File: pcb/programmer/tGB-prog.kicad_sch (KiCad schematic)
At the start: 34 parts, among them J1 ZX62R-B-5P, J2 PROG_PORT, U1 FT2232D, U2 93LC56BT-I/OT, U3 TPS79901DDCR, Y1 NX8045GB-6MHZ-STD-CSF-3

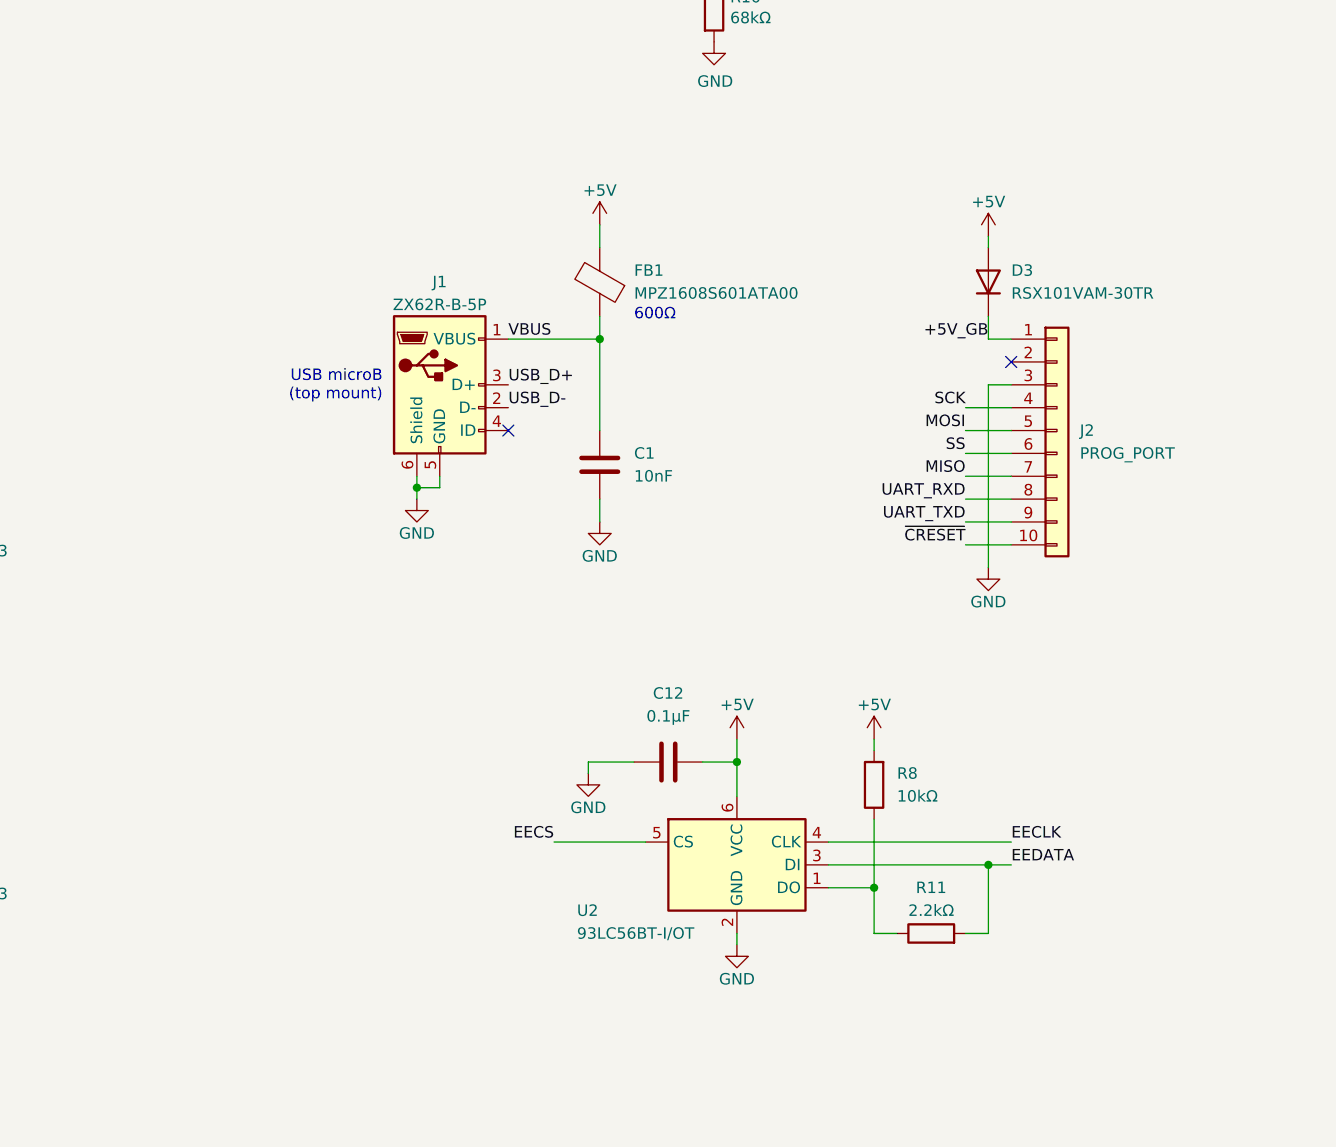
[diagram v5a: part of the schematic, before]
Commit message: add junpers for VDDIO supply from main board, add power LED
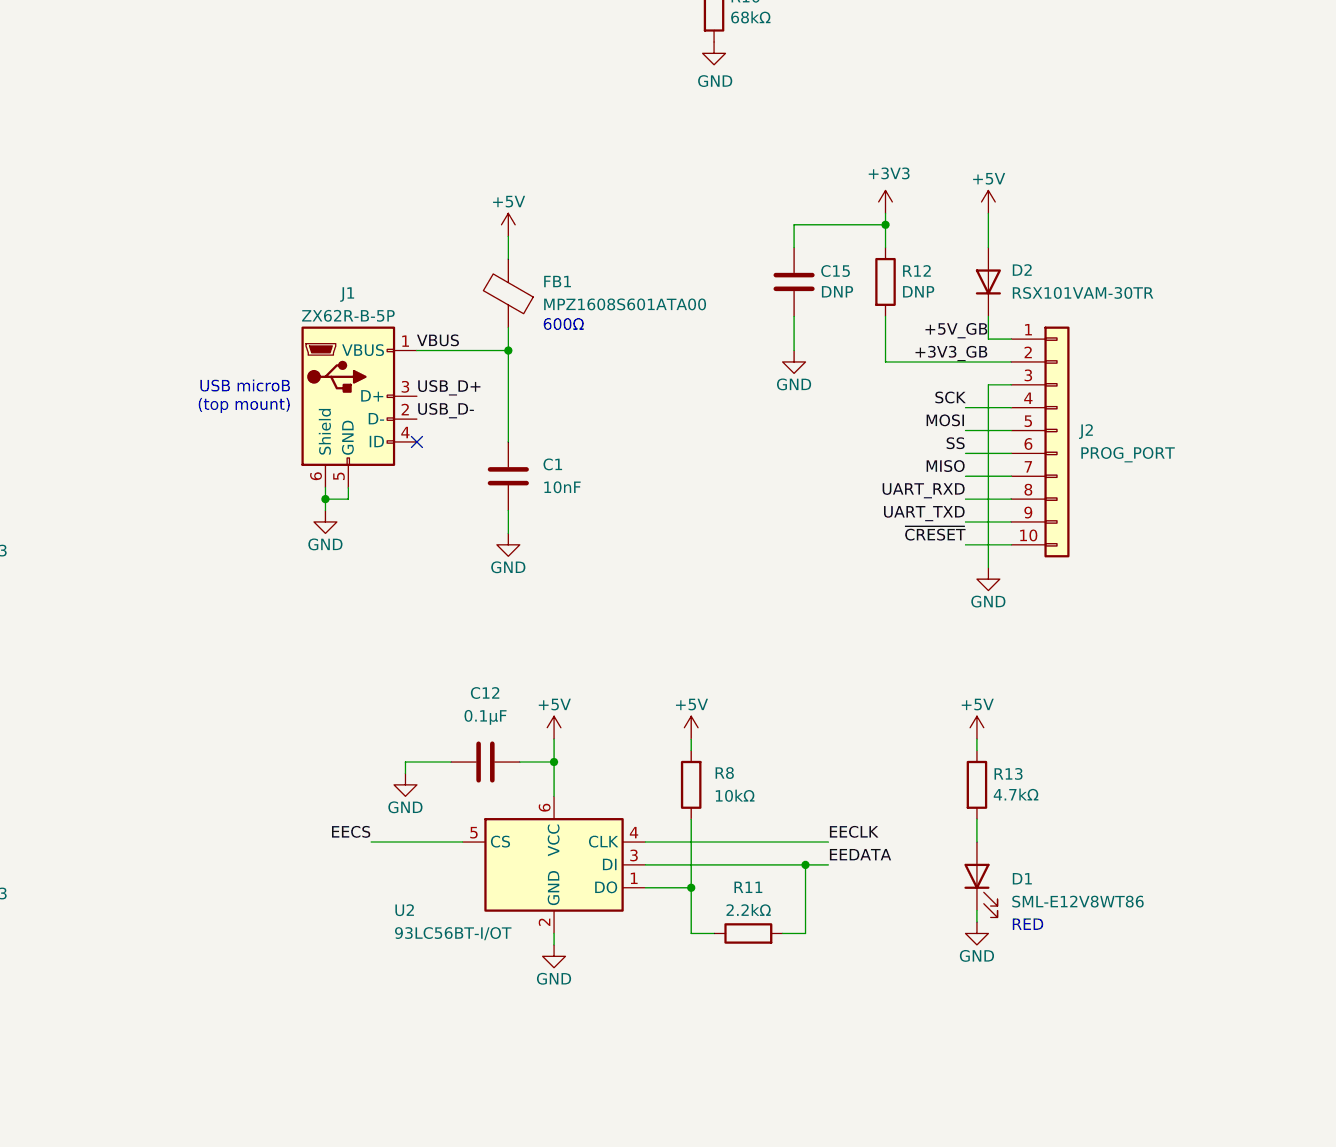
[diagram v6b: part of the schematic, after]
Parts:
- added C15: DNP, Capacitor_SMD:C_0603_1608Metric, symbol Device:C
- added D1: SML-E12V8WT86, LED_Addition:LED_0603_1608Metric_Castellated, symbol Device:LED
- added R12: DNP, Resistor_SMD:R_0603_1608Metric, symbol Device:R
- added R13: 4.7kΩ, Resistor_SMD:R_0402_1005Metric, symbol Device:R
- renumbered D3 to D2
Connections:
- net +3V3: now also C15.1, R12.1
- net +5V: now also R13.1
- net GND: now also C15.2, D1.1 (K)
- net +3V3_GB: now reaches J2.2 (Pin_2)
- net +3V3_GB: now also R12.2
- new net: D1.2 (A), R13.2
- no-connect marks 20 -> 19
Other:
- note added: "RED"
- moved on the sheet: C1, C12, FB1, J1, R11, R8, U2

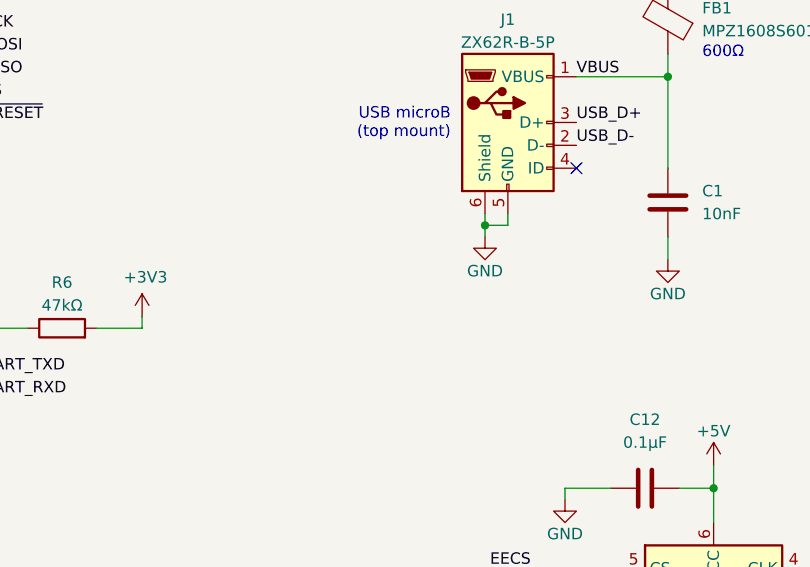
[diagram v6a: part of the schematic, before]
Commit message: separate USB GND and shield
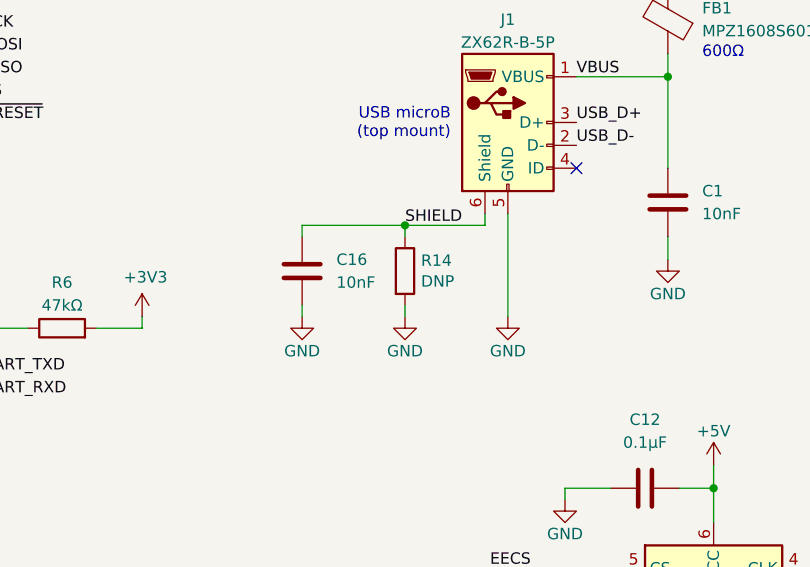
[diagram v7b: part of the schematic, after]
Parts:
- added C16: 10nF, Capacitor_SMD:C_0402_1005Metric, symbol Device:C
- added R14: DNP, Resistor_SMD:R_0402_1005Metric, symbol Device:R
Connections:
- net GND: now also C16.2, R14.2; no longer J1.6 (Shield)
- new net SHIELD: C16.1, J1.6 (Shield), R14.1
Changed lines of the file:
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@@
   (junction (at 232.41 31.75) (diameter 0) (color 0 0 0 0)
   )
+  (junction (at 168.91 105.41) (diameter 0) (color 0 0 0 0)
+  )
   (junction (at 99.06 168.91) (diameter 0) (color 0 0 0 0)
   )
@@
   )
   (junction (at 104.14 72.39) (diameter 0) (color 0 0 0 0)
-  )
-  (junction (at 177.8 105.41) (diameter 0) (color 0 0 0 0)
   )
   (junction (at 82.55 44.45) (diameter 0) (color 0 0 0 0)
@@
     (stroke (width 0) (type default) (color 0 0 0 0))
   )
-  (wire (pts (xy 180.34 105.41) (xy 177.8 105.41))
-    (stroke (width 0) (type default) (color 0 0 0 0))
-  )
   (wire (pts (xy 248.92 102.87) (xy 254 102.87))
     (stroke (width 0) (type default) (color 0 0 0 0))
@@
     (stroke (width 0) (type default) (color 0 0 0 0))
   )
+  (wire (pts (xy 157.48 105.41) (xy 168.91 105.41))
+    (stroke (width 0) (type default) (color 0 0 0 0))
+  )
   (wire (pts (xy 121.92 116.84) (xy 127 116.84))
     (stroke (width 0) (type default) (color 0 0 0 0))
@@
     (stroke (width 0) (type default) (color 0 0 0 0))
   )
-  (wire (pts (xy 177.8 105.41) (xy 177.8 106.68))
-    (stroke (width 0) (type default) (color 0 0 0 0))
-  )
   (wire (pts (xy 248.92 110.49) (xy 254 110.49))
     (stroke (width 0) (type default) (color 0 0 0 0))
@@
     (stroke (width 0) (type default) (color 0 0 0 0))
   )
+  (wire (pts (xy 168.91 105.41) (xy 168.91 106.68))
+    (stroke (width 0) (type default) (color 0 0 0 0))
+  )
   (wire (pts (xy 69.85 54.61) (xy 69.85 55.88))
     (stroke (width 0) (type default) (color 0 0 0 0))
@@
     (stroke (width 0) (type default) (color 0 0 0 0))
   )
+  (wire (pts (xy 177.8 104.14) (xy 177.8 105.41))
+    (stroke (width 0) (type default) (color 0 0 0 0))
+  )
   (wire (pts (xy 251.46 87.63) (xy 254 87.63))
     (stroke (width 0) (type default) (color 0 0 0 0))
@@
     (stroke (width 0) (type default) (color 0 0 0 0))
   )
+  (wire (pts (xy 157.48 114.3) (xy 157.48 115.57))
+    (stroke (width 0) (type default) (color 0 0 0 0))
+  )
   (wire (pts (xy 55.88 114.3) (xy 55.88 104.14))
     (stroke (width 0) (type default) (color 0 0 0 0))
@@
     (stroke (width 0) (type default) (color 0 0 0 0))
   )
-  (wire (pts (xy 177.8 104.14) (xy 177.8 105.41))
-    (stroke (width 0) (type default) (color 0 0 0 0))
-  )
   (wire (pts (xy 49.53 137.16) (xy 49.53 139.7))
     (stroke (width 0) (type default) (color 0 0 0 0))
   )
+  (wire (pts (xy 157.48 106.68) (xy 157.48 105.41))
+    (stroke (width 0) (type default) (color 0 0 0 0))
+  )
   (wire (pts (xy 49.53 119.38) (xy 49.53 118.11))
     (stroke (width 0) (type default) (color 0 0 0 0))
@@
     (stroke (width 0) (type default) (color 0 0 0 0))
   )
-  (wire (pts (xy 180.34 104.14) (xy 180.34 105.41))
+  (wire (pts (xy 180.34 104.14) (xy 180.34 115.57))
     (stroke (width 0) (type default) (color 0 0 0 0))
   )
@@
     (stroke (width 0) (type default) (color 0 0 0 0))
   )
+  (wire (pts (xy 177.8 105.41) (xy 168.91 105.41))
+    (stroke (width 0) (type default) (color 0 0 0 0))
+  )
   (wire (pts (xy 196.85 34.29) (xy 194.31 34.29))
+    (stroke (width 0) (type default) (color 0 0 0 0))
+  )
+  (wire (pts (xy 168.91 114.3) (xy 168.91 115.57))
     (stroke (width 0) (type default) (color 0 0 0 0))
   )
@@
   (label "3V3VO" (at 214.63 31.75 0)
     (effects (font (size 1.27 1.27)) (justify left bottom))
+  )
+  (label "SHIELD" (at 175.26 105.41 180)
+    (effects (font (size 1.27 1.27)) (justify right bottom))
   )
   (label "USB_D+" (at 40.64 104.14 180)
@@
     (pin "2")
   )
+  (symbol (lib_id "Device:R") (at 168.91 110.49 0) (unit 1)
+    (in_bom yes) (on_board yes)
+    (property "Reference" "R14" (id 0) (at 170.688 109.3216 0)
+      (effects (font (size 1.27 1.27)) (justify left))
+    )
+    (property "Value" "DNP" (id 1) (at 170.688 111.633 0)
+      (effects (font (size 1.27 1.27)) (justify left))
+    )
+    (property "Footprint" "Resistor_SMD:R_0402_1005Metric" (id 2) (at 167.132 110.49 90)
+      (effects (font (size 1.27 1.27)) hide)
+    )
+    (property "Datasheet" "~" (id 3) (at 168.91 110.49 0)
+      (effects (font (size 1.27 1.27)) hide)
+    )
+    (pin "1")
+    (pin "2")
+  )
   (symbol (lib_id "power:+5V") (at 218.44 132.08 0) (unit 1)
     (in_bom yes) (on_board yes)
@@
     (pin "2")
   )
+  (symbol (lib_id "power:GND") (at 168.91 115.57 0) (unit 1)
+    (in_bom yes) (on_board yes)
+    (property "Reference" "#PWR037" (id 0) (at 168.91 121.92 0)
+      (effects (font (size 1.27 1.27)) hide)
+    )
+    (property "Value" "GND" (id 1) (at 168.91 119.38 0))
+    (property "Footprint" "" (id 2) (at 168.91 115.57 0)
+      (effects (font (size 1.27 1.27)) hide)
+    )
+    (property "Datasheet" "" (id 3) (at 168.91 115.57 0)
+      (effects (font (size 1.27 1.27)) hide)
+    )
+    (pin "1")
+  )
   (symbol (lib_id "Device:C") (at 49.53 143.51 0) (unit 1)
     (in_bom yes) (on_board yes) (fields_autoplaced)
@@
     (pin "2")
   )
+  (symbol (lib_id "power:GND") (at 157.48 115.57 0) (unit 1)
+    (in_bom yes) (on_board yes)
+    (property "Reference" "#PWR038" (id 0) (at 157.48 121.92 0)
+      (effects (font (size 1.27 1.27)) hide)
+    )
+    (property "Value" "GND" (id 1) (at 157.48 119.38 0))
+    (property "Footprint" "" (id 2) (at 157.48 115.57 0)
+      (effects (font (size 1.27 1.27)) hide)
+    )
+    (property "Datasheet" "" (id 3) (at 157.48 115.57 0)
+      (effects (font (size 1.27 1.27)) hide)
+    )
+    (pin "1")
+  )
   (symbol (lib_id "power:PWR_FLAG") (at 330.2 0 180) (unit 1)
     (in_bom yes) (on_board yes) (fields_autoplaced)
@@
     (pin "1")
   )
-  (symbol (lib_id "power:GND") (at 177.8 106.68 0) (unit 1)
-    (in_bom yes) (on_board yes)
-    (property "Reference" "#PWR01" (id 0) (at 177.8 113.03 0)
-      (effects (font (size 1.27 1.27)) hide)
-    )
-    (property "Value" "GND" (id 1) (at 177.8 110.49 0))
-    (property "Footprint" "" (id 2) (at 177.8 106.68 0)
-      (effects (font (size 1.27 1.27)) hide)
-    )
-    (property "Datasheet" "" (id 3) (at 177.8 106.68 0)
+  (symbol (lib_id "power:GND") (at 180.34 115.57 0) (unit 1)
+    (in_bom yes) (on_board yes)
+    (property "Reference" "#PWR01" (id 0) (at 180.34 121.92 0)
+      (effects (font (size 1.27 1.27)) hide)
+    )
+    (property "Value" "GND" (id 1) (at 180.34 119.38 0))
+    (property "Footprint" "" (id 2) (at 180.34 115.57 0)
+      (effects (font (size 1.27 1.27)) hide)
+    )
+    (property "Datasheet" "" (id 3) (at 180.34 115.57 0)
       (effects (font (size 1.27 1.27)) hide)
     )
@@
     )
     (pin "1")
+  )
+  (symbol (lib_id "Device:C") (at 157.48 110.49 0) (mirror y) (unit 1)
+    (in_bom yes) (on_board yes) (fields_autoplaced)
+    (property "Reference" "C16" (id 0) (at 161.29 109.2199 0)
+      (effects (font (size 1.27 1.27)) (justify right))
+    )
+    (property "Value" "10nF" (id 1) (at 161.29 111.7599 0)
+      (effects (font (size 1.27 1.27)) (justify right))
+    )
+    (property "Footprint" "Capacitor_SMD:C_0402_1005Metric" (id 2) (at 156.5148 114.3 0)
+      (effects (font (size 1.27 1.27)) hide)
+    )
+    (property "Datasheet" "~" (id 3) (at 157.48 110.49 0)
+      (effects (font (size 1.27 1.27)) hide)
+    )
+    (pin "1")
+    (pin "2")
   )
   (symbol (lib_id "power:GND") (at 55.88 90.17 0) (unit 1)
@@
       (reference "#PWR036") (unit 1) (value "GND") (footprint "")
     )
+    (path "/4b91da05-04e7-46b5-9341-fcdb7da742db"
+      (reference "#PWR037") (unit 1) (value "GND") (footprint "")
+    )
+    (path "/6b37fc4e-71ea-472e-9193-936ad87aafa2"
+      (reference "#PWR038") (unit 1) (value "GND") (footprint "")
+    )
     (path "/e0087188-c787-4021-96c2-407ef2a614e6"
       (reference "C1") (unit 1) (value "10nF") (footprint "Capacitor_SMD:C_0402_1005Metric")
@@
       (reference "C15") (unit 1) (value "DNP") (footprint "Capacitor_SMD:C_0603_1608Metric")
     )
+    (path "/f4fb7369-a39f-4ac1-8fb6-911312380b03"
+      (reference "C16") (unit 1) (value "10nF") (footprint "Capacitor_SMD:C_0402_1005Metric")
+    )
     (path "/8337e039-7cfa-42a2-91fb-90365817b581"
       (reference "D1") (unit 1) (value "SML-E12V8WT86") (footprint "LED_Addition:LED_0603_1608Metric_Castellated")
@@
       (reference "R13") (unit 1) (value "4.7kΩ") (footprint "Resistor_SMD:R_0402_1005Metric")
     )
+    (path "/25a5bbdb-2959-4371-8033-149aaf664990"
+      (reference "R14") (unit 1) (value "DNP") (footprint "Resistor_SMD:R_0402_1005Metric")
+    )
     (path "/fc1e6fe4-e185-4f8c-8215-4a40401d71c9"

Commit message: add comments
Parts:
- C15: value DNP -> 4.7μF
- C16: value 10nF -> DNP
- R12: value DNP -> 0Ω
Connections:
- net +5V: now also FB1.1; no longer FB1.2
- net VBUS: now also FB1.2; no longer FB1.1
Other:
- note added: "Do not populate Reserved for VBUS(5V) to VDDIO(3.3V) generation"
- note added: "Optional EEPROM for FT2232 configuration (Not required)"
- moved on the sheet: C1, C10, C11, C12, C13, C14, C15, C16, D2, FB1, FB2, J1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
